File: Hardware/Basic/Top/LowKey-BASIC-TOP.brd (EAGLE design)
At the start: 38 x 38 mm, 51 parts, among them SW3 SWITCH.MOM, SW4 SWITCH.MOM, SW5 SWITCH.MOM, U1 NRF52832_MODULE_MDBT42, U2 FT231XS

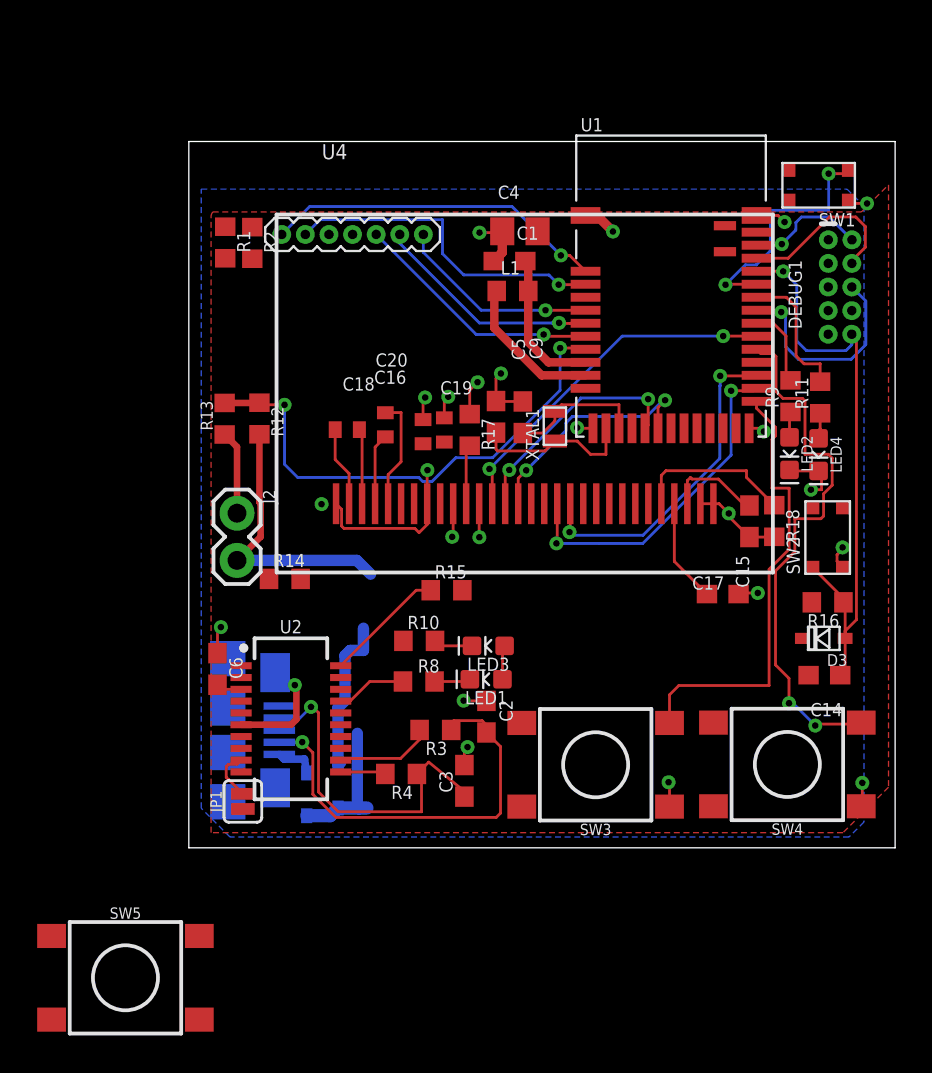
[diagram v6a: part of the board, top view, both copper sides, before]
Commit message: Finished routing top board
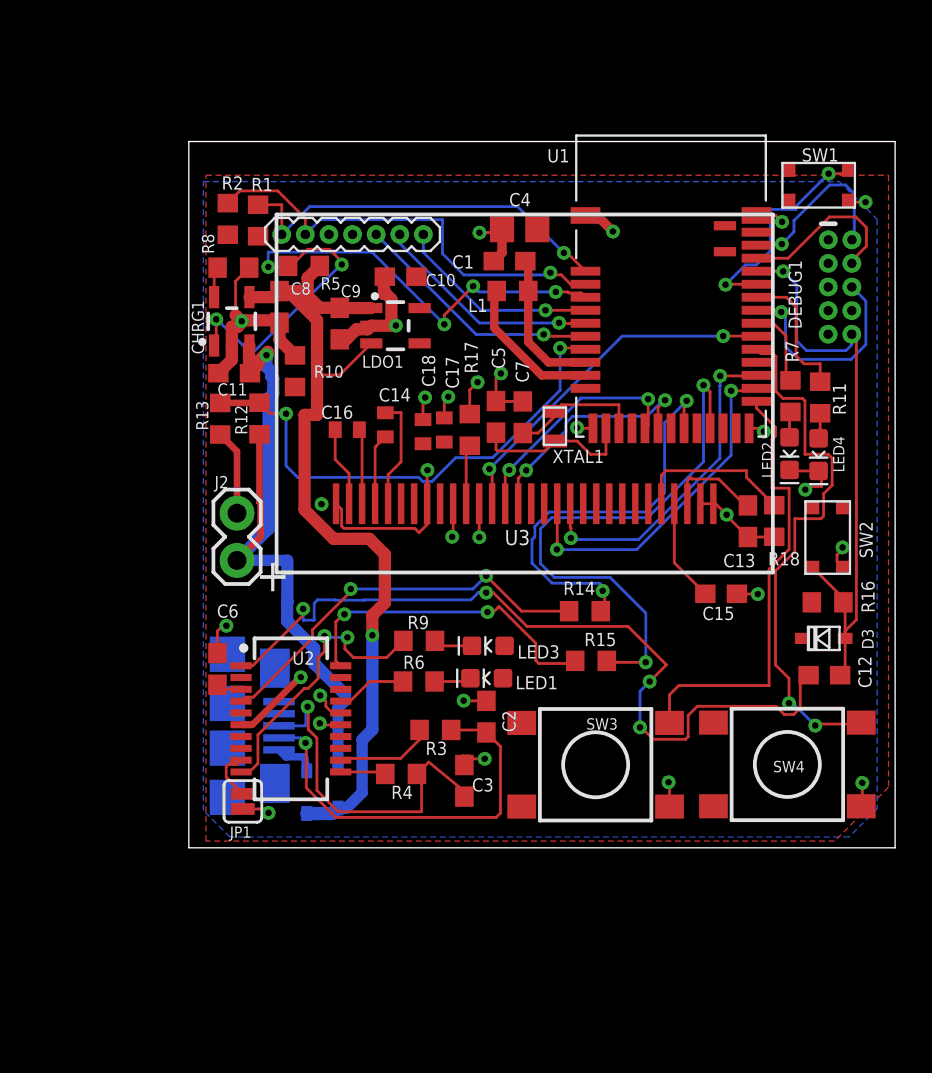
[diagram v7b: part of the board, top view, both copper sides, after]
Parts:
- removed C19, C20: 2.2uF, LinnesLab-Passives:C0402
- removed SW5: SWITCH.MOM, LinnesLab-Switches:TACTILE_SWITCH_SMD_6.2MM_TALL
- added C10: 1u, LinnesLab-Passives:C0603
- added C11, C8: 4.7u, LinnesLab-Passives:C0603
- added C12: 100n, LinnesLab-Passives:C0603
- added C13: 10uF, LinnesLab-Passives:C0603
- added C7: (no value), LinnesLab-Passives:C0603
- added CHRG1: MCP73831, LinnesLab-Power:SOT23-5
- added LDO1: MIC5504, LinnesLab-Power:SOT23-5
- added R5: 100k, LinnesLab-Passives:R0603
- added R6, R7: 1k, LinnesLab-Passives:R0603
- C14: value 100n -> 2.2uF; device LinnesLab-Passives:C0603 -> LinnesLab-Passives:C0402
- C15: value 10uF -> 2.2uF
- C17: device LinnesLab-Passives:C0603 -> LinnesLab-Passives:C0402
- C9: value (none) -> 1u
- R10: value 1k -> 100k
- R8: value 1k -> (none)
- moved C14 27.2 mm to (10.6, 22.8), turned to 270 degrees
- moved R8 24.4 mm to (2.40, 31.2), turned to 180 degrees
- moved R9 23.9 mm to (12.4, 11.1), turned to 0 degrees
- moved C17 17.4 mm to (13.7, 22.5), turned to 270 degrees
- moved R14 16.2 mm to (21.3, 12.7)
- moved R10 16.0 mm to (5.71, 25.6), turned to 270 degrees
- moved C9 11.1 mm to (8.12, 28.2)
- moved R15 8.65 mm to (21.6, 10.1)
- moved C15 4.19 mm to (28.6, 13.7), turned to 180 degrees
- moved C18 4.08 mm to (12.6, 22.4), turned to 270 degrees
- moved R1 2.13 mm to (3.73, 33.7)
- moved C16 2.06 mm to (8.53, 22.5), turned to 180 degrees
- moved R2 1.84 mm to (2.10, 33.8)
- moved USB1 0.24 mm to (3.35, 6.57)
- moved R13 0.24 mm to (1.69, 23.1)
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- renumbered U4 to U3
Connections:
- removed net D27/CHRG.STATUS: U1.4
- removed net SW3: SW5.A1, SW5.A2
- new net D27/CHRG.STAT: CHRG1.1, R5.1, U1.4
- new net N$17: CHRG1.5, R8.2
- net 3.3V: now also C10.1, C17.2, C18.2, LDO1.5, R10.2; no longer C19.2, C20.2
- net DTR: now also C12.1; no longer C14.1
- net GND: now also C10.2, C11.2, C13.1, C18.1, C7.2, C8.1, C9.1, CHRG1.2, LDO1.2, R10.1, R8.1; no longer C19.1, C20.1, C9.2, SW5.B1, SW5.B2
- net LED1: now also R7.2; no longer R9.2
- net N$13: now also C13.2; no longer C15.2
- net N$15: now also C15.2; no longer C17.2
- net N$3: now also C16.2; no longer C18.2
- net N$31: now also R6.2; no longer R8.2
- net N$32: now also R9.2; no longer R10.2
- net N$5: now also C16.1; no longer C18.1
- net N$6: now also C7.1; no longer C9.1
- net N$7: now also C14.2; no longer C16.2
- net N$8: now also C14.1; no longer C16.1
- net N$9: now also R7.1; no longer R9.1
- net RESET: now also C12.2; no longer C14.2
- net RXLED: now also R6.1; no longer R8.1
- net TXLED: now also R9.1; no longer R10.1
- net VIN: now also C8.2, C9.2, CHRG1.4, LDO1.1, LDO1.3, R5.2
- net VLIPO: now also C11.1, CHRG1.3
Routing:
- net DTR: track 0.00 -> 44.3 mm, vias 0 -> 4
- net VIN: track 7.46 -> 47.8 mm, vias 0 -> 1
- net D27/CHRG.STAT: track 0.00 -> 36.7 mm, vias 0 -> 6
- net RXD.NRF: track 0.00 -> 30.3 mm, vias 0 -> 2
- net TXD.NRF: track 0.00 -> 22.6 mm, vias 0 -> 2
- net GND: track 56.1 -> 78.0 mm, vias 24 -> 28
- net RXD.FT: track 0.00 -> 21.6 mm, vias 0 -> 2
- net TXLED: track 0.23 -> 15.3 mm, vias 0 -> 2
- net VLIPO: track 23.4 -> 38.1 mm, vias 0 -> 1
- net TXD.FT: track 6.53 -> 17.6 mm, vias 0 -> 2
- net SCL: track 17.9 -> 24.0 mm
- net SWDIO: track 6.51 -> 9.69 mm
- net SDA: track 18.4 -> 21.3 mm
- net 3.3V: track 3.22 -> 1.37 mm
- net N$17: track 0.00 -> 1.67 mm
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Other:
- board text added: "+"
